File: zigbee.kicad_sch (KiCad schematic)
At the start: 12 parts, among them J13 mrf24j40_tp, J14 mrf24j40_tp, U4 MRF24J40MA

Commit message: Fix KiCad 10 footprint library: register kiC library, fix schematic references
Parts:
- U4: footprint MODULE_MRF24J40MA -> kiC:MODULE_MRF24J40MA
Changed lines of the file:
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@@
 			)
 		)
-		(property "Footprint" "MODULE_MRF24J40MA"
+		(property "Footprint" "kiC:MODULE_MRF24J40MA"
 			(at 137.16 78.74 0)
 			(hide yes)

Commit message: feat: PCB layout updates, schematic changes, fp-lib-table config
- cnc_pic32.kicad_pcb: component repositioning, board outline, text formatting
- cnc_pic32.kicad_prl/pro: project settings updates
- fp-lib-table: add Library path to Library.pretty
- mcu.kicad_sch: PIC32 pin configuration updates
- zigbee.kicad_sch: MRF24J40 module updates
- oscilator.kicad_sch: crystal configuration
- power.kicad_sch/power_ft232.kicad_sch: power supply updates
- oled.kicad_sch: OLED display connections
- idc.kicad_sch: IDC connector updates
- osc_ft232.kicad_sch: FT232 crystal
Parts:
- U5: renamed from U4; footprint kiC:MODULE_MRF24J40MA -> Library:MODULE_MRF24J40MA
- renumbered C22 to C27, C23 to C28, J13 to J15, J14 to J16, R32 to R31, R33 to R32, R34 to R33, R35 to R34, R36 to R35, R37 to R36, R38 to R37
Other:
- moved on the sheet: J15

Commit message: feat: integrate zigbee sheet + R 0603→0805 footprint update
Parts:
- R35: renamed from R33; footprint Resistor_SMD:R_0603_1608Metric -> Resistor_SMD:R_0805_2012Metric
- renumbered J15 to J23, J16 to J24, R31 to R33, R32 to R34, R34 to R36, R35 to R37, R36 to R38, R37 to R39

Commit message: feat: 2-layer stackup, bus net class and schematic cleanup
PCB / project
- Reduce board from 4 layers to 2 (F.Cu / B.Cu) for cheaper fabrication
- Add "bus" net class and reorder net class priorities (bus 0, usb_differential 1, ...)

Schematics
- usb_conector_Ft232: add D+ / D-- labels on the USB mini-B data pair
- ft232: add 10K pull-ups, 100nf decoupling and test points on +3.3VA
- tp_ft232: remove solder jumpers JP1/JP2 (TX_Rpi / RX_Rpi now direct)
- Usb_pic32: add C38 100nf decoupling on +5V
- oled: expand connector J25 from 7 to 8 pins
- mcu / idc / power / zigbee / buttons / cnc_pic32: annotation and net cleanup

docs
- Add USB-Mini-B pinout reference images
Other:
- moved on the sheet: J24, R35, R36, R37, R38, R39

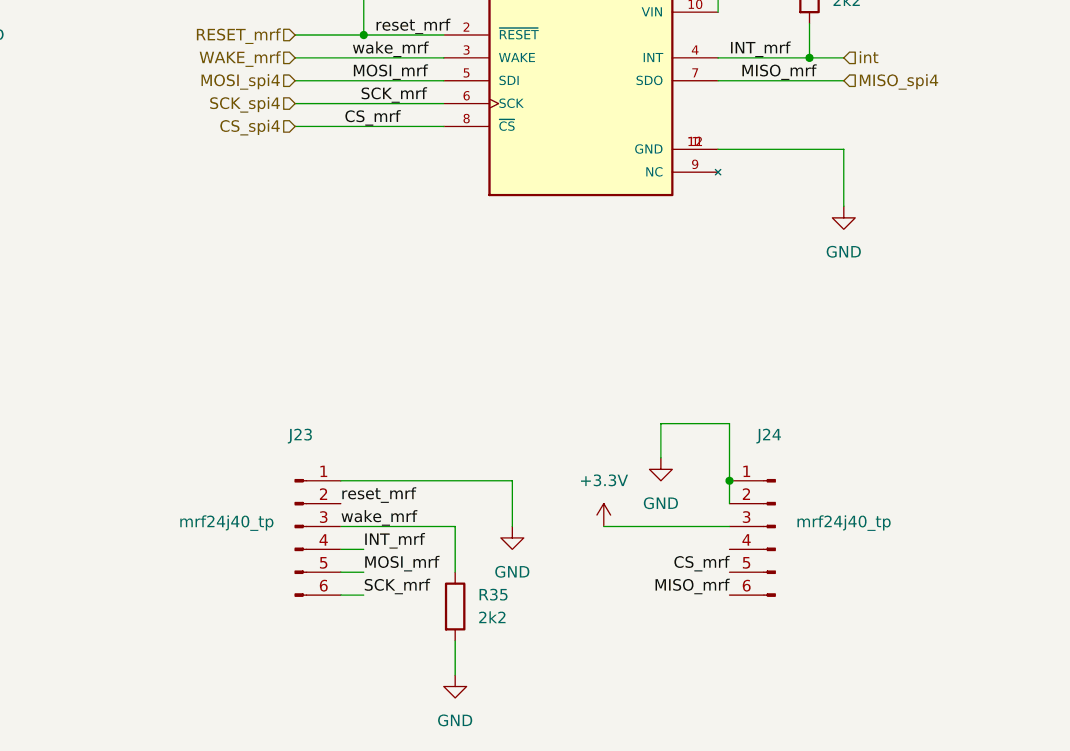
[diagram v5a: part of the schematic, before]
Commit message: feat: add MA240011 module sheet with labeled pins + Altium socket footprint
Esquemático
- Nueva hoja hija MA240011.kicad_sch (módulo PIC32 TQFP-100) referenciada
  desde la hoja MA240011 de mcu.kicad_sch
- mcu.kicad_sch: los 83 pines jerárquicos de MA240011 quedan rotulados con un
  label local del mismo nombre; 81 de ellos con un tramo de wire de 2.54 mm
  (un label solo no conecta a un pin de hoja) y RD4/RD5 sobre el wire existente
- mcu.kicad_sch: borde derecho del sheet 104.775 -> 106.68 mm y sus 41 pines,
  para quedar en grilla de 1.27 mm (evita 41 avisos endpoint_off_grid)
- ERC: 341 -> 158 violaciones; pin_not_connected 120 -> 39,
  isolated_pin_label 113 -> 10, endpoint_off_grid 6 -> 6
- power / zigbee / oled / pololu / cnc_pic32: pines MS1-MS3, conectores y
  anotacion de netnames

PCB
- Referencia de los 132 footprints a size 0.8 x 0.8 mm y thickness 0.12 mm
  (render_cache obsoleto eliminado para forzar el re-render)

Footprints
- lib/altium.pretty/MA240011_Socket_TQFP100_100pin.kicad_mod: zocalo adaptador
  de 100 pines TH pitch 1.27 mm convertido desde altium/Multimedia/MM20141127.PcbDoc
  (J4, patron MA240011); pads girados 90 grados sentido horario
- fp-lib-table: alta de la biblioteca "altium" (${KIPRJMOD}/lib/altium.pretty)

.gitignore
- Ignorar altium/, tmp/ y *.bkp (backups de KiCad)
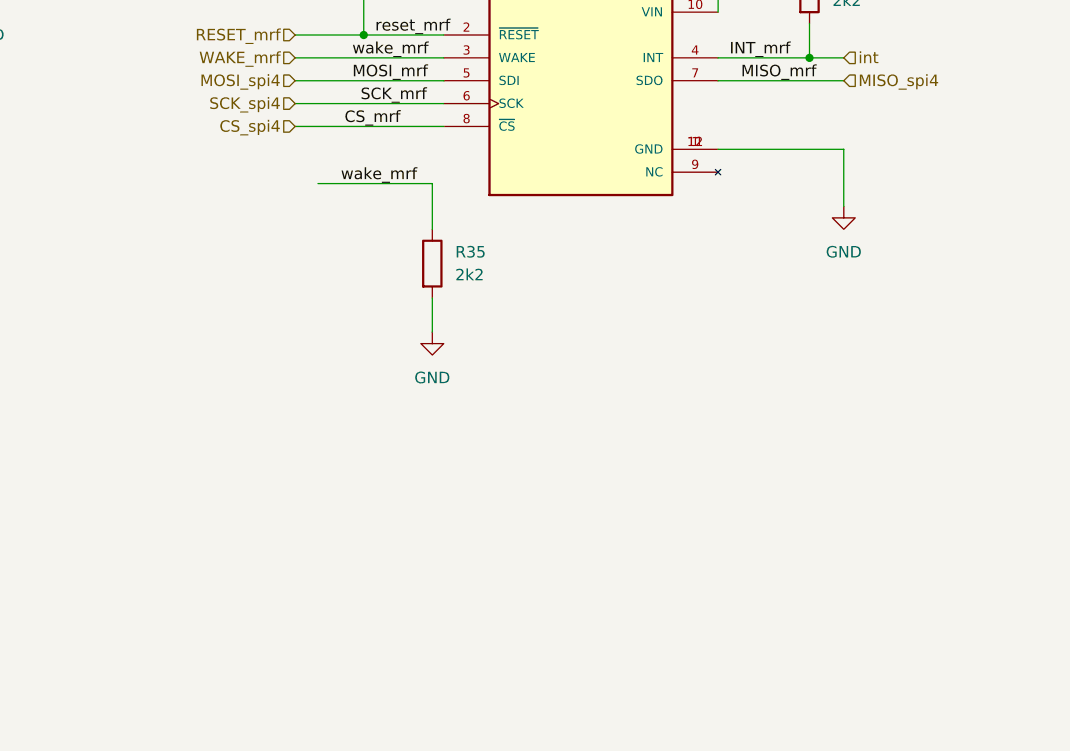
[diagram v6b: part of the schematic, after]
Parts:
- removed J23, J24: mrf24j40_tp, Connector_PinHeader_2.54mm:PinHeader_1x06_P2.54mm_Vertical, symbol Connector:Conn_01x06_Pin
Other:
- moved on the sheet: R35

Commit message: add files
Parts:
- removed U5: MRF24J40MA, Library:MODULE_MRF24J40MA, symbol RF_ZigBee:MRF24J40MA
- added D3, D4, D5: LED, Diode_SMD:D_0805_2012Metric, symbol Device:LED
- added R40, R41: 1k, Resistor_SMD:R_0805_2012Metric, symbol Device:R
- added U8: ESP8266-12E_ESP-12E, RF_Module:ESP-12E, symbol ESP8266-12E_ESP-12E:ESP8266-12E_ESP-12E
- R35: value 2k2 -> 1k
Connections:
- net +3.3V: now also U8.8 (VCC)
- net CS_spi4: now also U8.9 (CS0)
- net GND: now also R40.2, R41.2, U8.15 (GND)
- net MISO_spi4: now also U8.10 (MISO)
- net MOSI_spi4: now also U8.13 (MOSI)
- net RESET_mrf: now also U8.1 (RESET)
- net SCK_spi4: now also U8.14 (SCLK)
- net WAKE_mrf: now also U8.3 (EN); no longer R35.1
- new net: D3.1 (K), R35.1
- new net: D3.2 (A), U8.4 (IO16)
- new net: D4.1 (K), R40.1
- new net: D4.2 (A), U8.16 (IO15)
- new net: D5.2 (A), U8.5 (IO14)
- new net: D5.1 (K), R41.1
- new net RXD_ESP8266: U8.21 (RXD)
- new net TXD_ESP8266: U8.22 (TXD)
- no-connect marks 0 -> 9
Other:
- moved on the sheet: R35

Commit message: updated
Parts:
- C27, C28: footprint Capacitor_SMD:C_0805_2012Metric -> Resistor_SMD:R_0603_1608Metric
- D3, D4, D5, U8: now left out of the parts list
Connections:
- net CS_spi4 renamed CS_esp8266
- net MISO_spi4 renamed MISO_esp8266
- net MOSI_spi4 renamed MOSI_esp8266
- net SCK_spi4 renamed SCK_esp8266
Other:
- moved on the sheet: D3, D4, D5, R35, R40, R41, U8
